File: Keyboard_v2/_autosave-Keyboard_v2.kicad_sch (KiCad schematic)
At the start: 177 parts, among them SW1 SW_Push, U1 ATmega32U4-A, Y1 16MHz

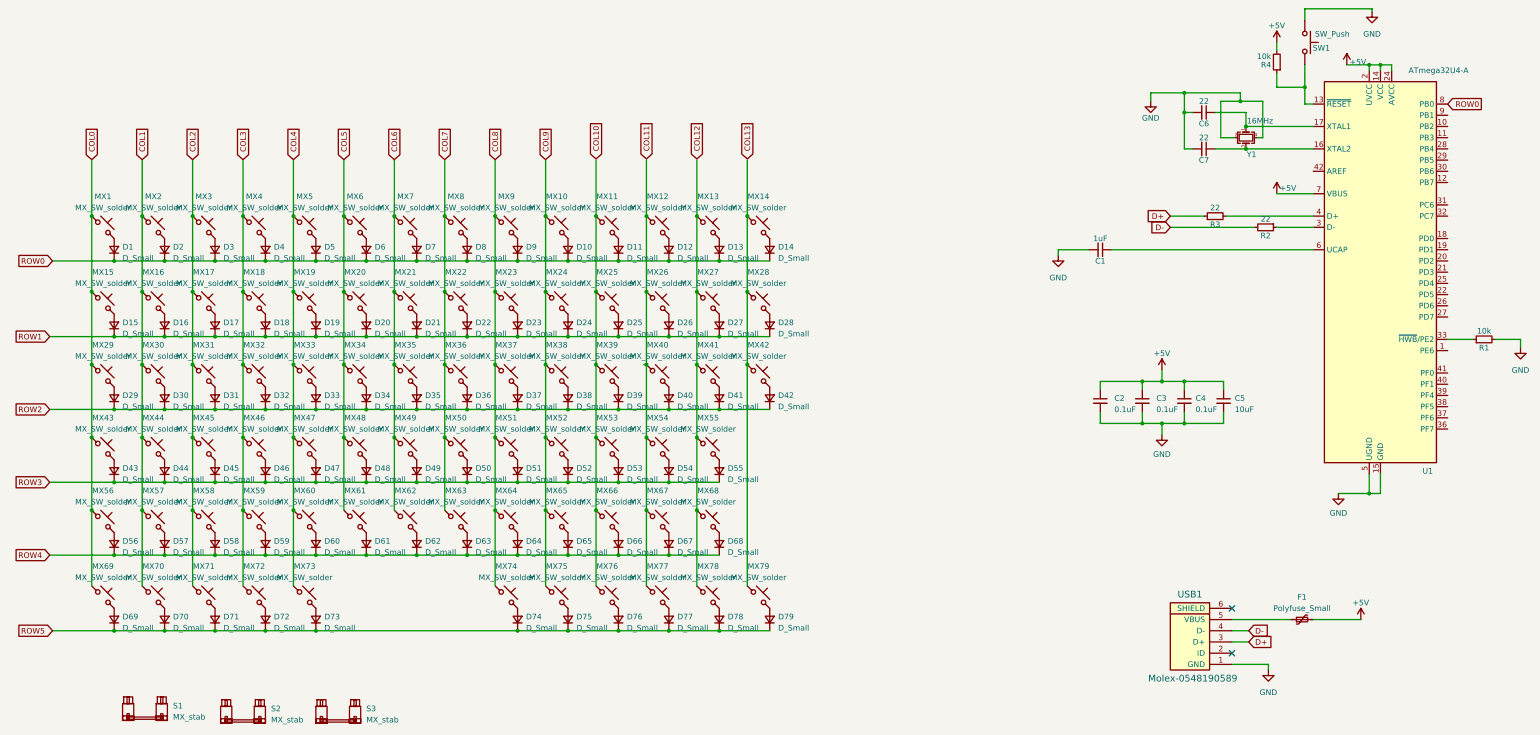
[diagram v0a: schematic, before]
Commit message: pcb is routed and ground fills added
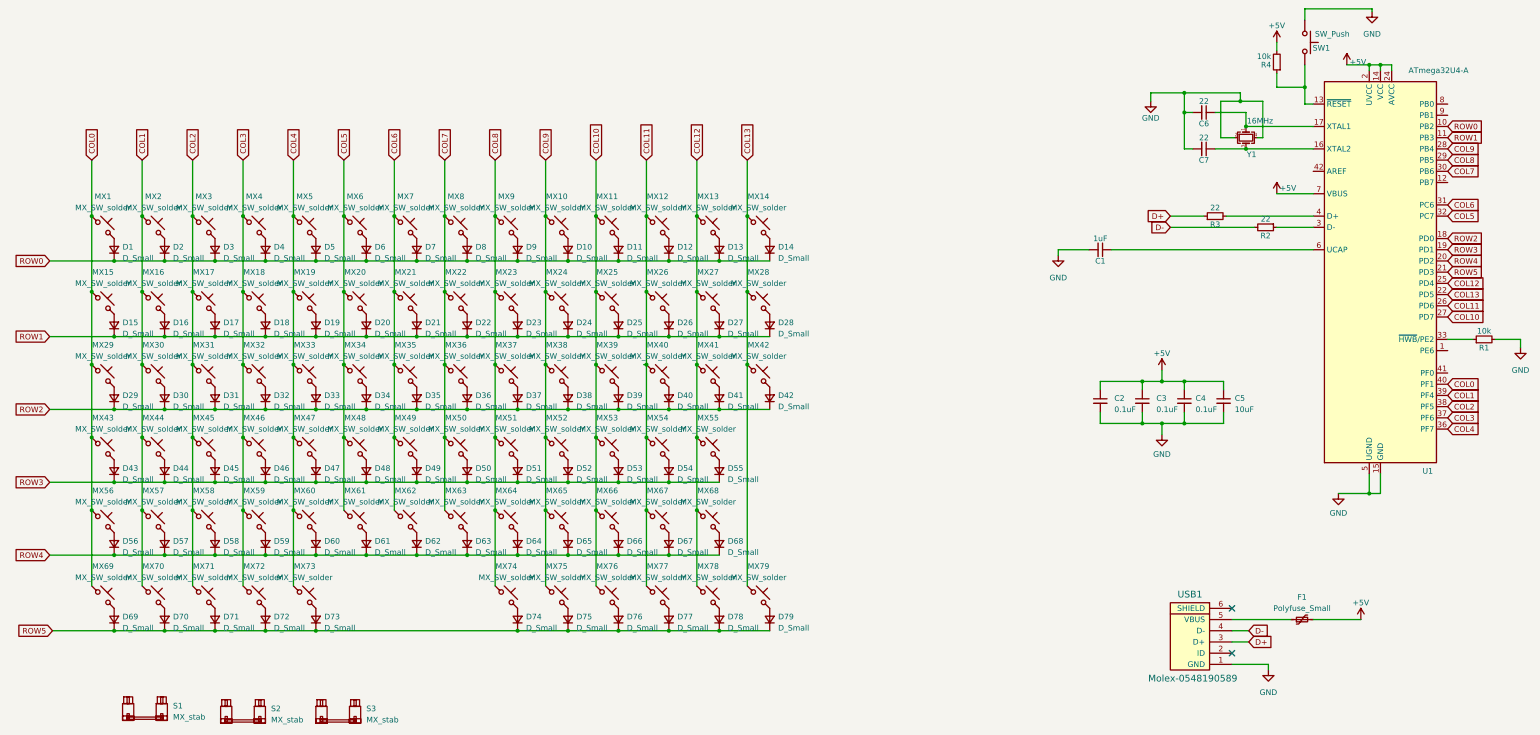
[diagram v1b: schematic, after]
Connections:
- net COL0: now also MX1.1, MX15.1, MX29.1, MX43.1, MX56.1, MX69.1, U1.40 (PF1)
- net COL1: now also MX16.1, MX2.1, MX30.1, MX44.1, MX57.1, MX70.1, U1.39 (PF4)
- net COL10: now also MX11.1, MX25.1, MX39.1, MX53.1, MX66.1, MX76.1, U1.27 (PD7)
- net COL11: now also MX12.1, MX26.1, MX40.1, MX54.1, MX67.1, MX77.1, U1.26 (PD6)
- net COL12: now also MX13.1, MX27.1, MX41.1, MX55.1, MX68.1, MX78.1, U1.25 (PD4)
- net COL13: now also MX14.1, MX28.1, MX42.1, MX79.1, U1.22 (PD5)
- net COL2: now also MX17.1, MX3.1, MX31.1, MX45.1, MX58.1, MX71.1, U1.38 (PF5)
- net COL3: now also MX18.1, MX32.1, MX4.1, MX46.1, MX59.1, MX72.1, U1.37 (PF6)
- net COL4: now also MX19.1, MX33.1, MX47.1, MX5.1, MX60.1, MX73.1, U1.36 (PF7)
- net COL5: now also MX20.1, MX34.1, MX48.1, MX6.1, MX61.1, U1.32 (PC7)
- net COL6: now also MX21.1, MX35.1, MX49.1, MX62.1, MX7.1, U1.31 (PC6)
- net COL7: now also MX22.1, MX36.1, MX50.1, MX63.1, MX8.1, U1.30 (PB6)
- net COL8: now also MX23.1, MX37.1, MX51.1, MX64.1, MX74.1, MX9.1, U1.29 (PB5)
- net COL9: now also MX10.1, MX24.1, MX38.1, MX52.1, MX65.1, MX75.1, U1.28 (PB4)
- net ROW0: now also D1.1 (K), D10.1 (K), D11.1 (K), D12.1 (K), D13.1 (K), D14.1 (K), D2.1 (K), D3.1 (K), D4.1 (K), D5.1 (K), D6.1 (K), D7.1 (K), D8.1 (K), D9.1 (K), U1.10 (PB2)
- net ROW1: now also D15.1 (K), D16.1 (K), D17.1 (K), D18.1 (K), D19.1 (K), D20.1 (K), D21.1 (K), D22.1 (K), D23.1 (K), D24.1 (K), D25.1 (K), D26.1 (K), D27.1 (K), D28.1 (K), U1.11 (PB3)
- net ROW2: now also D29.1 (K), D30.1 (K), D31.1 (K), D32.1 (K), D33.1 (K), D34.1 (K), D35.1 (K), D36.1 (K), D37.1 (K), D38.1 (K), D39.1 (K), D40.1 (K), D41.1 (K), D42.1 (K), U1.18 (PD0)
- net ROW3: now also D43.1 (K), D44.1 (K), D45.1 (K), D46.1 (K), D47.1 (K), D48.1 (K), D49.1 (K), D50.1 (K), D51.1 (K), D52.1 (K), D53.1 (K), D54.1 (K), D55.1 (K), U1.19 (PD1)
- net ROW4: now also D56.1 (K), D57.1 (K), D58.1 (K), D59.1 (K), D60.1 (K), D61.1 (K), D62.1 (K), D63.1 (K), D64.1 (K), D65.1 (K), D66.1 (K), D67.1 (K), D68.1 (K), U1.20 (PD2)
- net ROW5: now also D69.1 (K), D70.1 (K), D71.1 (K), D72.1 (K), D73.1 (K), D74.1 (K), D75.1 (K), D76.1 (K), D77.1 (K), D78.1 (K), D79.1 (K), U1.21 (PD3)
